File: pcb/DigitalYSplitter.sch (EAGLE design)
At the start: 40 parts, among them CN1 Battery, CON1 USB_MICROSMT+THRUHULE, CON2 M05X2NO_SILK, CON3 LED_OUT, CON5 LED_OUT, Q1 16MHz, SW1 BUTTON_1, SW2 BUTTON_2, U1 MK20D--VFM5, U3 74LVC1G17DCK, U4 74LVC1G17DCK, U5 74LVC1G17DCK, U6 TPD4S012, U7 74LVC1G17DCK

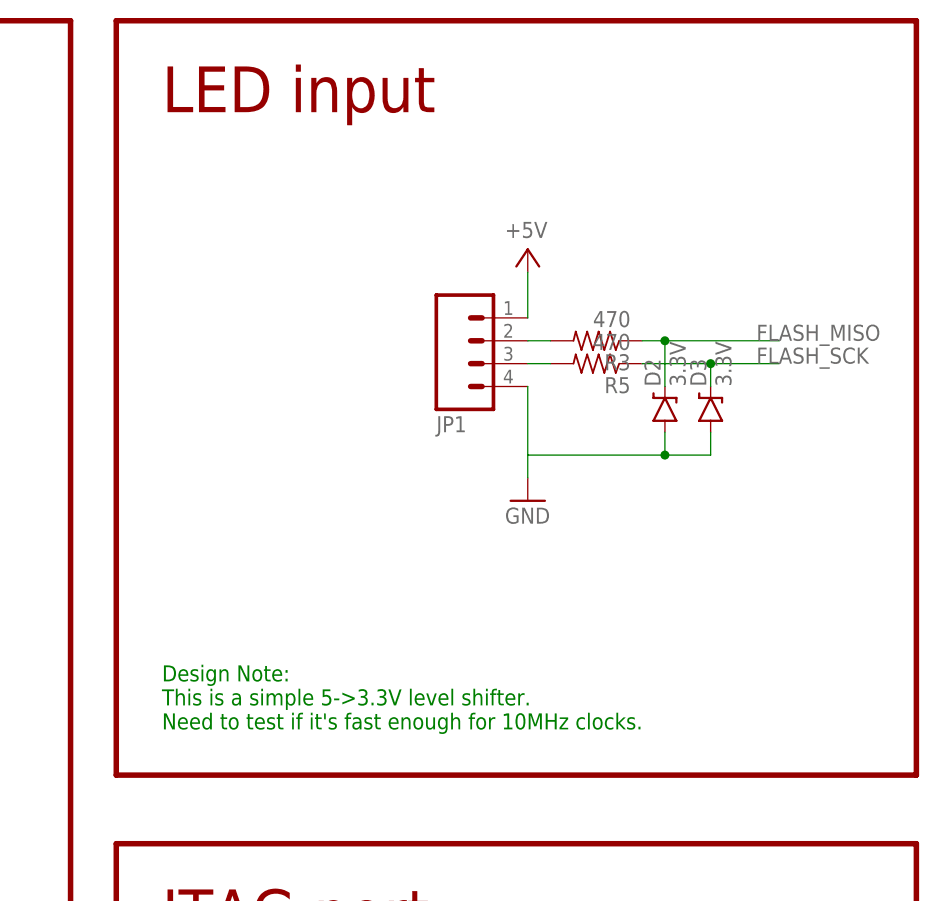
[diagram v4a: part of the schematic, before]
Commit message: Schematic bugfix: can't use diodes for level shifting, they're too slow.
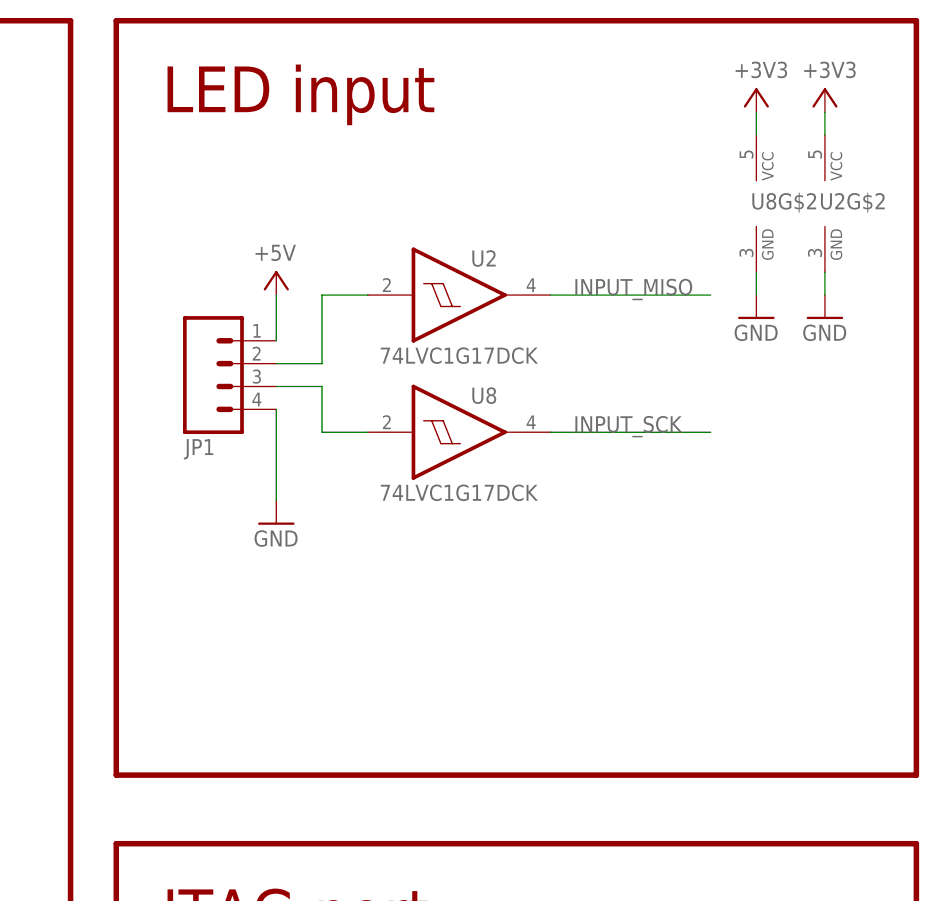
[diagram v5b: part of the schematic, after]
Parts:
- removed D2, D3: 3.3V, SparkFun-DiscreteSemi:DIODE-ZENER3.3V
- removed R3, R5: 470, adafruit:R-US_R0402
- added U2, U8: 74LVC1G17DCK, 74xx-little-us:74LVC1G17DCK
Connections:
- removed net FLASH_MISO: D2.C, R3.1
- removed net FLASH_SCK: D3.C, R5.1
- net +3V3: now also U2G$2.VCC, U8G$2.VCC
- net GND: now also U2G$2.GND, U8G$2.GND; no longer D2.A, D3.A
- net INPUT_MISO: now also U2G$1.O
- net INPUT_SCK: now also U8G$1.O
- net N$6: now also U2G$1.I; no longer R3.2
- net N$8: now also U8G$1.I; no longer R5.2
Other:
- note removed: "Design Note: This is a simple 5->3.3V level shifter. Need to test if it's fast enough for 10MHz clocks."
- moved on the sheet: JP1
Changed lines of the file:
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@@
 <part name="P+8" library="supply1" deviceset="+5V" device=""/>
 <part name="JP1" library="SparkFun-Connectors" deviceset="M04" device="PTH"/>
-<part name="R3" library="adafruit" deviceset="R-US_" device="R0402" value="470"/>
-<part name="R5" library="adafruit" deviceset="R-US_" device="R0402" value="470"/>
-<part name="D2" library="SparkFun-DiscreteSemi" deviceset="DIODE-ZENER" device="3.3V" value="3.3V"/>
-<part name="D3" library="SparkFun-DiscreteSemi" deviceset="DIODE-ZENER" device="3.3V" value="3.3V"/>
 <part name="R6" library="adafruit" deviceset="R-US_" device="R0402" value="470"/>
 <part name="LED2" library="adafruit" deviceset="LED" device="CHIPLED_0805" value="STATUS"/>
@@
 <part name="LED0" library="adafruit" deviceset="LED" device="CHIPLED_0805" value="STATUS"/>
 <part name="3V7" library="supply1" deviceset="+3V3" device=""/>
+<part name="U2" library="74xx-little-us" deviceset="74*1G17" device="DCK" technology="LVC"/>
+<part name="GND16" library="supply1" deviceset="GND" device=""/>
+<part name="U8" library="74xx-little-us" deviceset="74*1G17" device="DCK" technology="LVC"/>
+<part name="GND17" library="supply1" deviceset="GND" device=""/>
+<part name="3V3" library="supply1" deviceset="+3V3" device=""/>
+<part name="3V8" library="supply1" deviceset="+3V3" device=""/>
 </parts>
 <sheets>
@@
 <wire x1="251.46" y1="35.56" x2="251.46" y2="-48.26" width="0.6096" layer="94"/>
 <text x="109.22" y="25.4" size="5.08" layer="94">Output B</text>
-<text x="261.62" y="170.18" size="1.778" layer="91">Design Note:
-This is a simple 5-&gt;3.3V level shifter.
-Need to test if it's fast enough for 10MHz clocks.</text>
 </plain>
 <instances>
@@
 <instance part="GND9" gate="1" x="124.46" y="200.66"/>
 <instance part="GND15" gate="1" x="81.28" y="205.74"/>
-<instance part="GND10" gate="1" x="302.26" y="195.58"/>
+<instance part="GND10" gate="1" x="274.32" y="193.04"/>
 <instance part="C1" gate="G$1" x="66.04" y="215.9"/>
 <instance part="GND12" gate="1" x="35.56" y="78.74"/>
@@
 <instance part="GND14" gate="1" x="116.84" y="-15.24"/>
 <instance part="CON5" gate="1" x="233.68" y="-22.86" rot="R180"/>
-<instance part="P+8" gate="1" x="302.26" y="223.52" smashed="yes">
-<attribute name="VALUE" x="299.72" y="224.79" size="1.778" layer="96"/>
-</instance>
-<instance part="JP1" gate="G$1" x="297.18" y="213.36" rot="MR180"/>
-<instance part="R3" gate="G$1" x="309.88" y="213.36" rot="R180"/>
-<instance part="R5" gate="G$1" x="309.88" y="210.82" rot="R180"/>
-<instance part="D2" gate="G$1" x="317.5" y="205.74" rot="R90"/>
-<instance part="D3" gate="G$1" x="322.58" y="205.74" rot="R90"/>
+<instance part="P+8" gate="1" x="274.32" y="220.98" smashed="yes">
+<attribute name="VALUE" x="271.78" y="222.25" size="1.778" layer="96"/>
+</instance>
+<instance part="JP1" gate="G$1" x="269.24" y="210.82" rot="MR180"/>
 <instance part="R6" gate="G$1" x="55.88" y="0" rot="R90"/>
 <instance part="LED2" gate="G$1" x="55.88" y="-10.16"/>
@@
 <instance part="3V7" gate="G$1" x="30.48" y="10.16" smashed="yes">
 <attribute name="VALUE" x="27.94" y="11.43" size="1.778" layer="96"/>
+</instance>
+<instance part="U2" gate="G$1" x="294.64" y="218.44" smashed="yes">
+<attribute name="NAME" x="295.91" y="221.615" size="1.778" layer="95"/>
+<attribute name="VALUE" x="285.75" y="210.82" size="1.778" layer="96"/>
+</instance>
+<instance part="U2" gate="G$2" x="335.28" y="228.6"/>
+<instance part="GND16" gate="1" x="335.28" y="215.9"/>
+<instance part="U8" gate="G$1" x="294.64" y="203.2" smashed="yes">
+<attribute name="NAME" x="295.91" y="206.375" size="1.778" layer="95"/>
+<attribute name="VALUE" x="285.75" y="195.58" size="1.778" layer="96"/>
+</instance>
+<instance part="U8" gate="G$2" x="327.66" y="228.6"/>
+<instance part="GND17" gate="1" x="327.66" y="215.9"/>
+<instance part="3V3" gate="G$1" x="327.66" y="241.3" smashed="yes">
+<attribute name="VALUE" x="325.12" y="242.57" size="1.778" layer="96"/>
+</instance>
+<instance part="3V8" gate="G$1" x="335.28" y="241.3" smashed="yes">
+<attribute name="VALUE" x="332.74" y="242.57" size="1.778" layer="96"/>
 </instance>
 </instances>
@@
 <pinref part="GND10" gate="1" pin="GND"/>
 <pinref part="JP1" gate="G$1" pin="4"/>
-<wire x1="302.26" y1="208.28" x2="302.26" y2="200.66" width="0.1524" layer="91"/>
-<pinref part="D3" gate="G$1" pin="A"/>
-<wire x1="302.26" y1="200.66" x2="302.26" y2="198.12" width="0.1524" layer="91"/>
-<wire x1="322.58" y1="203.2" x2="322.58" y2="200.66" width="0.1524" layer="91"/>
-<wire x1="322.58" y1="200.66" x2="317.5" y2="200.66" width="0.1524" layer="91"/>
-<pinref part="D2" gate="G$1" pin="A"/>
-<wire x1="317.5" y1="200.66" x2="302.26" y2="200.66" width="0.1524" layer="91"/>
-<wire x1="317.5" y1="203.2" x2="317.5" y2="200.66" width="0.1524" layer="91"/>
-<junction x="317.5" y="200.66"/>
+<wire x1="274.32" y1="205.74" x2="274.32" y2="195.58" width="0.1524" layer="91"/>
+</segment>
+<segment>
+<pinref part="U2" gate="G$2" pin="GND"/>
+<pinref part="GND16" gate="1" pin="GND"/>
+<wire x1="335.28" y1="218.44" x2="335.28" y2="220.98" width="0.1524" layer="91"/>
+</segment>
+<segment>
+<pinref part="U8" gate="G$2" pin="GND"/>
+<pinref part="GND17" gate="1" pin="GND"/>
+<wire x1="327.66" y1="220.98" x2="327.66" y2="218.44" width="0.1524" layer="91"/>
 </segment>
 </net>
@@
 <pinref part="JP1" gate="G$1" pin="1"/>
 <pinref part="P+8" gate="1" pin="+5V"/>
-<wire x1="302.26" y1="220.98" x2="302.26" y2="215.9" width="0.1524" layer="91"/>
+<wire x1="274.32" y1="218.44" x2="274.32" y2="213.36" width="0.1524" layer="91"/>
 </segment>
 </net>
@@
 <wire x1="30.48" y1="7.62" x2="30.48" y2="5.08" width="0.1524" layer="91"/>
 </segment>
+<segment>
+<pinref part="U8" gate="G$2" pin="VCC"/>
+<wire x1="327.66" y1="236.22" x2="327.66" y2="238.76" width="0.1524" layer="91"/>
+<pinref part="3V3" gate="G$1" pin="+3V3"/>
+</segment>
+<segment>
+<pinref part="U2" gate="G$2" pin="VCC"/>
+<wire x1="335.28" y1="238.76" x2="335.28" y2="236.22" width="0.1524" layer="91"/>
+<pinref part="3V8" gate="G$1" pin="+3V3"/>
+</segment>
 </net>
 <net name="TCLK" class="0">
@@
 </segment>
 </net>
-<net name="FLASH_SCK" class="0">
-<segment>
-<wire x1="314.96" y1="210.82" x2="322.58" y2="210.82" width="0.1524" layer="91"/>
-<label x="327.66" y="210.82" size="1.778" layer="95"/>
-<pinref part="D3" gate="G$1" pin="C"/>
-<wire x1="322.58" y1="210.82" x2="330.2" y2="210.82" width="0.1524" layer="91"/>
-<wire x1="322.58" y1="210.82" x2="322.58" y2="208.28" width="0.1524" layer="91"/>
-<junction x="322.58" y="210.82"/>
-<pinref part="R5" gate="G$1" pin="1"/>
-</segment>
-</net>
 <net name="INPUT_MOSI" class="0">
 <segment>
@@
 <wire x1="205.74" y1="177.8" x2="187.96" y2="177.8" width="0.1524" layer="91"/>
 <label x="195.58" y="177.8" size="1.778" layer="95"/>
-</segment>
-</net>
-<net name="FLASH_MISO" class="0">
-<segment>
-<wire x1="330.2" y1="213.36" x2="317.5" y2="213.36" width="0.1524" layer="91"/>
-<label x="327.66" y="213.36" size="1.778" layer="95"/>
-<pinref part="D2" gate="G$1" pin="C"/>
-<wire x1="317.5" y1="213.36" x2="314.96" y2="213.36" width="0.1524" layer="91"/>
-<wire x1="317.5" y1="213.36" x2="317.5" y2="208.28" width="0.1524" layer="91"/>
-<junction x="317.5" y="213.36"/>
-<pinref part="R3" gate="G$1" pin="1"/>
 </segment>
 </net>
@@
 <segment>
 <pinref part="JP1" gate="G$1" pin="2"/>
-<pinref part="R3" gate="G$1" pin="2"/>
-<wire x1="304.8" y1="213.36" x2="302.26" y2="213.36" width="0.1524" layer="91"/>
+<wire x1="274.32" y1="210.82" x2="279.4" y2="210.82" width="0.1524" layer="91"/>
+<wire x1="279.4" y1="210.82" x2="279.4" y2="218.44" width="0.1524" layer="91"/>
+<pinref part="U2" gate="G$1" pin="I"/>
+<wire x1="279.4" y1="218.44" x2="284.48" y2="218.44" width="0.1524" layer="91"/>
 </segment>
 </net>
@@
 <segment>
 <pinref part="JP1" gate="G$1" pin="3"/>
-<pinref part="R5" gate="G$1" pin="2"/>
-<wire x1="304.8" y1="210.82" x2="302.26" y2="210.82" width="0.1524" layer="91"/>
+<pinref part="U8" gate="G$1" pin="I"/>
+<wire x1="284.48" y1="203.2" x2="279.4" y2="203.2" width="0.1524" layer="91"/>
+<wire x1="279.4" y1="203.2" x2="279.4" y2="208.28" width="0.1524" layer="91"/>
+<wire x1="279.4" y1="208.28" x2="274.32" y2="208.28" width="0.1524" layer="91"/>
 </segment>
 </net>
@@
 <label x="195.58" y="180.34" size="1.778" layer="95"/>
 </segment>
+<segment>
+<pinref part="U8" gate="G$1" pin="O"/>
+<wire x1="304.8" y1="203.2" x2="322.58" y2="203.2" width="0.1524" layer="91"/>
+<label x="307.34" y="203.2" size="1.778" layer="95"/>
+</segment>
 </net>
 <net name="INPUT_MISO" class="0">
@@
 <label x="195.58" y="175.26" size="1.778" layer="95"/>
 </segment>
-</net>
+<segment>
+<pinref part="U2" gate="G$1" pin="O"/>
+<wire x1="304.8" y1="218.44" x2="322.58" y2="218.44" width="0.1524" layer="91"/>
+<label x="307.34" y="218.44" size="1.778" layer="95"/>
+</segment>
+</net>
